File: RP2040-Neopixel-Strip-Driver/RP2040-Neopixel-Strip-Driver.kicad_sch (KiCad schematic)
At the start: 2 parts, among them U101 NLSX4302EBMUTCG

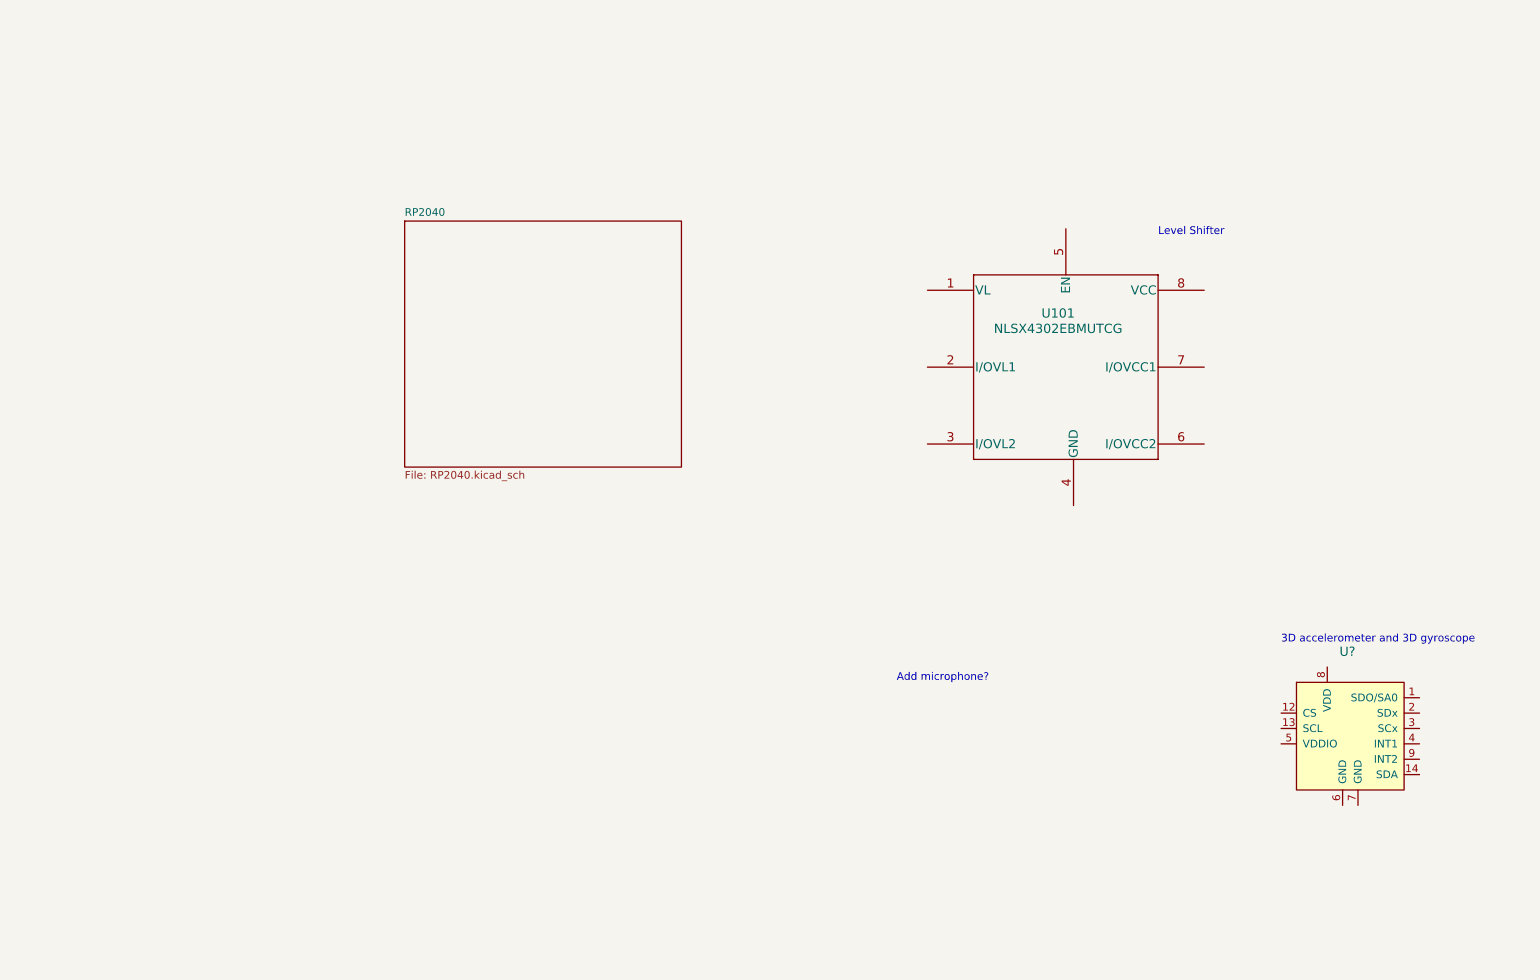
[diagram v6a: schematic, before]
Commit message: Project Expansion/Pivot - This is now a very involved cosplay prop tool.
Looking to incorporate a lot:
3D Gyro + 3D Accelerometer
Neopixel Driver
Speaker Driver
Microphone
SD Card Connector
Battery
Etc.
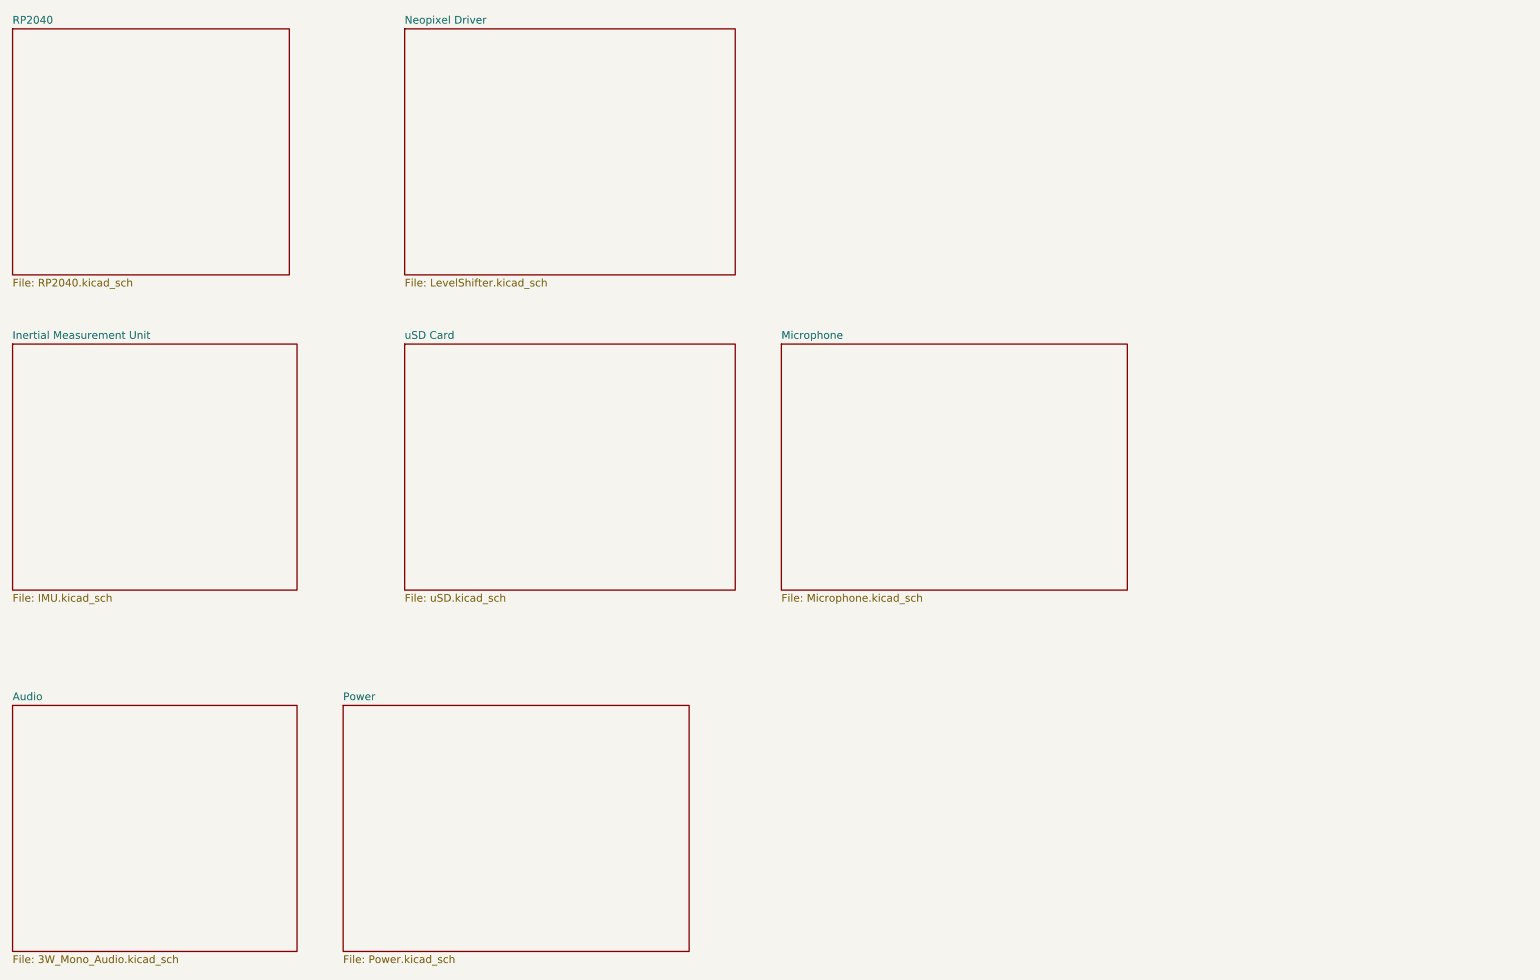
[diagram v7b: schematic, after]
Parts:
- removed U101: NLSX4302EBMUTCG, NLSX4302EBMUTCG:NLSX4302EBMUTCG, symbol NLSX4302EBMUTCG:NLSX4302EBMUTCG
- removed U?: (no value), symbol dk_Motion-Sensors-IMUs-Inertial-Measurement-Units:LSM6DS3TR
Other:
- added sheet Audio (3W_Mono_Audio.kicad_sch)
- added sheet Inertial Measurement Unit (IMU.kicad_sch)
- added sheet Microphone (Microphone.kicad_sch)
- added sheet Neopixel Driver (LevelShifter.kicad_sch)
- added sheet Power (Power.kicad_sch)
- added sheet uSD Card (uSD.kicad_sch)
- note removed: "3D accelerometer and 3D gyroscope"
- note removed: "Add microphone?"
- note removed: "Level Shifter"
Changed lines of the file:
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@@
     (comment 4 "https://github.com/mrangen/RP2040-Dev-Board")
   )
-  (text "Add microphone?" (at 163.83 127 0)
-    (effects (font (size 1.27 1.27)) (justify left bottom))
-  )
-  (text "Level Shifter\n" (at 207.01 53.34 0)
-    (effects (font (size 1.27 1.27)) (justify left bottom))
-  )
-  (text "3D accelerometer and 3D gyroscope" (at 227.33 120.65 0)
-    (effects (font (size 1.27 1.27)) (justify left bottom))
-  )
-  (symbol (lib_id "NLSX4302EBMUTCG:NLSX4302EBMUTCG") (at 168.91 67.31 0) (unit 1)
-    (in_bom yes) (on_board yes) (fields_autoplaced)
-    (property "Reference" "U101" (id 0) (at 190.5 66.04 0)
-      (effects (font (size 1.524 1.524)))
-    )
-    (property "Value" "NLSX4302EBMUTCG" (id 1) (at 190.5 68.58 0)
-      (effects (font (size 1.524 1.524)))
-    )
-    (property "Footprint" "NLSX4302EBMUTCG:NLSX4302EBMUTCG" (id 2) (at 191.77 58.674 0)
-      (effects (font (size 1.524 1.524)) hide)
-    )
-    (property "Datasheet" "" (id 3) (at 168.91 67.31 0)
-      (effects (font (size 1.524 1.524)))
-    )
-    (property "JLCPCB P/N" "C893527" (id 4) (at 168.91 67.31 0)
-      (effects (font (size 1.27 1.27)) hide)
-    )
-    (pin "1")
-    (pin "2")
-    (pin "3")
-    (pin "4")
-    (pin "5")
-    (pin "6")
-    (pin "7")
-    (pin "8")
-  )
-  (symbol (lib_id "dk_Motion-Sensors-IMUs-Inertial-Measurement-Units:LSM6DS3TR") (at 237.49 137.16 0) (unit 1)
-    (in_bom yes) (on_board yes) (fields_autoplaced)
-    (property "Reference" "U?" (id 0) (at 236.9694 121.92 0)
-      (effects (font (size 1.524 1.524)) (justify left))
-    )
-    (property "Value" "" (id 1) (at 236.9694 125.73 0)
-      (effects (font (size 1.524 1.524)) (justify left))
-    )
-    (property "Footprint" "" (id 2) (at 242.57 132.08 0)
-      (effects (font (size 1.524 1.524)) (justify left) hide)
-    )
-    (property "Datasheet" "http://www.st.com/content/ccc/resource/technical/document/datasheet/a3/f5/4f/ae/8e/44/41/d7/DM00133076.pdf/files/DM00133076.pdf/jcr:content/translations/en.DM00133076.pdf" (id 3) (at 242.57 129.54 0)
-      (effects (font (size 1.524 1.524)) (justify left) hide)
-    )
-    (property "Digi-Key_PN" "497-15383-1-ND" (id 4) (at 242.57 127 0)
-      (effects (font (size 1.524 1.524)) (justify left) hide)
-    )
-    (property "MPN" "LSM6DS3TR" (id 5) (at 242.57 124.46 0)
-      (effects (font (size 1.524 1.524)) (justify left) hide)
-    )
-    (property "Category" "Sensors, Transducers" (id 6) (at 242.57 121.92 0)
-      (effects (font (size 1.524 1.524)) (justify left) hide)
-    )
-    (property "Family" "Motion Sensors - IMUs (Inertial Measurement Units)" (id 7) (at 242.57 119.38 0)
-      (effects (font (size 1.524 1.524)) (justify left) hide)
-    )
-    (property "DK_Datasheet_Link" "http://www.st.com/content/ccc/resource/technical/document/datasheet/a3/f5/4f/ae/8e/44/41/d7/DM00133076.pdf/files/DM00133076.pdf/jcr:content/translations/en.DM00133076.pdf" (id 8) (at 242.57 116.84 0)
-      (effects (font (size 1.524 1.524)) (justify left) hide)
-    )
-    (property "DK_Detail_Page" "/product-detail/en/stmicroelectronics/LSM6DS3TR/497-15383-1-ND/5180534" (id 9) (at 242.57 114.3 0)
-      (effects (font (size 1.524 1.524)) (justify left) hide)
-    )
-    (property "Description" "IMU ACCEL/GYRO I2C/SPI 14VFLGA" (id 10) (at 242.57 111.76 0)
-      (effects (font (size 1.524 1.524)) (justify left) hide)
-    )
-    (property "Manufacturer" "STMicroelectronics" (id 11) (at 242.57 109.22 0)
-      (effects (font (size 1.524 1.524)) (justify left) hide)
-    )
-    (property "Status" "Active" (id 12) (at 242.57 106.68 0)
-      (effects (font (size 1.524 1.524)) (justify left) hide)
-    )
-    (property "JLCPCB P/N" "C967633" (id 13) (at 237.49 137.16 0)
-      (effects (font (size 1.27 1.27)) hide)
-    )
-    (pin "1")
-    (pin "10")
-    (pin "11")
-    (pin "12")
-    (pin "13")
-    (pin "14")
-    (pin "2")
-    (pin "3")
-    (pin "4")
-    (pin "5")
-    (pin "6")
-    (pin "7")
-    (pin "8")
-    (pin "9")
-  )
-  (sheet (at 82.55 50.8) (size 45.72 40.64) (fields_autoplaced)
-    (stroke (width 0.1524) (type solid) (color 0 0 0 0))
-    (fill (color 0 0 0 0.0000))
-    (property "Sheet name" "RP2040" (id 0) (at 82.55 50.0884 0)
-      (effects (font (size 1.27 1.27)) (justify left bottom))
-    )
-    (property "Sheet file" "RP2040.kicad_sch" (id 1) (at 82.55 92.0246 0)
+  (sheet (at 17.78 130.81) (size 46.99 40.64) (fields_autoplaced)
+    (stroke (width 0.1524) (type solid) (color 0 0 0 0))
+    (fill (color 0 0 0 0.0000))
+    (property "Sheet name" "Audio" (id 0) (at 17.78 130.0984 0)
+      (effects (font (size 1.27 1.27)) (justify left bottom))
+    )
+    (property "Sheet file" "3W_Mono_Audio.kicad_sch" (id 1) (at 17.78 172.0346 0)
+      (effects (font (size 1.27 1.27)) (justify left top))
+    )
+  )
+  (sheet (at 72.39 130.81) (size 57.15 40.64) (fields_autoplaced)
+    (stroke (width 0.1524) (type solid) (color 0 0 0 0))
+    (fill (color 0 0 0 0.0000))
+    (property "Sheet name" "Power" (id 0) (at 72.39 130.0984 0)
+      (effects (font (size 1.27 1.27)) (justify left bottom))
+    )
+    (property "Sheet file" "Power.kicad_sch" (id 1) (at 72.39 172.0346 0)
+      (effects (font (size 1.27 1.27)) (justify left top))
+    )
+  )
+  (sheet (at 17.78 19.05) (size 45.72 40.64) (fields_autoplaced)
+    (stroke (width 0.1524) (type solid) (color 0 0 0 0))
+    (fill (color 0 0 0 0.0000))
+    (property "Sheet name" "RP2040" (id 0) (at 17.78 18.3384 0)
+      (effects (font (size 1.27 1.27)) (justify left bottom))
+    )
+    (property "Sheet file" "RP2040.kicad_sch" (id 1) (at 17.78 60.2746 0)
+      (effects (font (size 1.27 1.27)) (justify left top))
+    )
+  )
+  (sheet (at 17.78 71.12) (size 46.99 40.64) (fields_autoplaced)
+    (stroke (width 0.1524) (type solid) (color 0 0 0 0))
+    (fill (color 0 0 0 0.0000))
+    (property "Sheet name" "Inertial Measurement Unit" (id 0) (at 17.78 70.4084 0)
+      (effects (font (size 1.27 1.27)) (justify left bottom))
+    )
+    (property "Sheet file" "IMU.kicad_sch" (id 1) (at 17.78 112.3446 0)
+      (effects (font (size 1.27 1.27)) (justify left top))
+    )
+  )
+  (sheet (at 82.55 19.05) (size 54.61 40.64) (fields_autoplaced)
+    (stroke (width 0.1524) (type solid) (color 0 0 0 0))
+    (fill (color 0 0 0 0.0000))
+    (property "Sheet name" "Neopixel Driver" (id 0) (at 82.55 18.3384 0)
+      (effects (font (size 1.27 1.27)) (justify left bottom))
+    )
+    (property "Sheet file" "LevelShifter.kicad_sch" (id 1) (at 82.55 60.2746 0)
+      (effects (font (size 1.27 1.27)) (justify left top))
+    )
+  )
+  (sheet (at 144.78 71.12) (size 57.15 40.64) (fields_autoplaced)
+    (stroke (width 0.1524) (type solid) (color 0 0 0 0))
+    (fill (color 0 0 0 0.0000))
+    (property "Sheet name" "Microphone" (id 0) (at 144.78 70.4084 0)
+      (effects (font (size 1.27 1.27)) (justify left bottom))
+    )
+    (property "Sheet file" "Microphone.kicad_sch" (id 1) (at 144.78 112.3446 0)
+      (effects (font (size 1.27 1.27)) (justify left top))
+    )
+  )
+  (sheet (at 82.55 71.12) (size 54.61 40.64) (fields_autoplaced)
+    (stroke (width 0.1524) (type solid) (color 0 0 0 0))
+    (fill (color 0 0 0 0.0000))
+    (property "Sheet name" "uSD Card" (id 0) (at 82.55 70.4084 0)
+      (effects (font (size 1.27 1.27)) (justify left bottom))
+    )
+    (property "Sheet file" "uSD.kicad_sch" (id 1) (at 82.55 112.3446 0)
       (effects (font (size 1.27 1.27)) (justify left top))
     )
@@
     (path "/" (page "1"))
     (path "/3e7bcc2a-10c2-45cd-9897-4c0007e1c7fc" (page "2"))
+    (path "/70fbb85f-3163-4abc-9c0a-a891d94f22b1" (page "3"))
+    (path "/0a22e777-1680-4ad6-bc95-a4eb9dcd85fc" (page "4"))
+    (path "/0df4e21b-e0d5-4c43-99fc-07b3ff9e029e" (page "5"))
+    (path "/f6d3734f-f3ae-47ca-9988-e728219f2f3d" (page "6"))
+    (path "/7d3ce60b-0fbc-4d1c-8ad6-57910cd4368e" (page "7"))
+    (path "/84db7bec-6432-452c-8477-921546ad9ffb" (page "8"))
   )
   (symbol_instances
@@
       (reference "J206") (unit 1) (value "GND") (footprint "Connector_PinSocket_2.54mm:PinSocket_1x01_P2.54mm_Vertical")
     )
+    (path "/f6d3734f-f3ae-47ca-9988-e728219f2f3d/a52ed90b-9977-491a-b2c3-312cce74a18b"
+      (reference "MICRO_SD?") (unit 1) (value "TF-01A") (footprint "TF-01A")
+    )
     (path "/3e7bcc2a-10c2-45cd-9897-4c0007e1c7fc/97c99fad-afb5-471e-b90a-b7f0de492c8f"
       (reference "R201") (unit 1) (value "1k") (footprint "Breadstick Footprints:Perfect_0402_Resistor")
@@
       (reference "SW202") (unit 1) (value "~{USB_BOOT}") (footprint "Breadstick Footprints:GT-TC029B-H025-L1N")
     )
-    (path "/61abfe14-530f-45cb-bac5-bff48de16e05"
-      (reference "U101") (unit 1) (value "NLSX4302EBMUTCG") (footprint "NLSX4302EBMUTCG:NLSX4302EBMUTCG")
-    )
     (path "/3e7bcc2a-10c2-45cd-9897-4c0007e1c7fc/00c3344e-81e0-498f-aca3-32f690281efd"
       (reference "U201") (unit 1) (value "XC6206P332MR") (footprint "Package_TO_SOT_SMD:SOT-23")
@@
       (reference "U205") (unit 1) (value "W25Q128JVPIQ") (footprint "Package_SON:WSON-8-1EP_6x5mm_P1.27mm_EP3.4x4.3mm")
     )
-    (path "/e57cd689-f3bf-4a84-b820-dd33af7d6263"
+    (path "/70fbb85f-3163-4abc-9c0a-a891d94f22b1/cdfffdd0-a453-4bd1-a6a1-94448da82674"
       (reference "U?") (unit 1) (value "LSM6DS3TR") (footprint "digikey-footprints:LGA-14L_2.5x3mm__LSM6DS3")
     )
+    (path "/7d3ce60b-0fbc-4d1c-8ad6-57910cd4368e/fde06394-20cf-471d-939a-9b94cd877da7"
+      (reference "U?") (unit 1) (value "NLSX4302EBMUTCG") (footprint "NLSX4302EBMUTCG:NLSX4302EBMUTCG")
+    )
     (path "/3e7bcc2a-10c2-45cd-9897-4c0007e1c7fc/2a22be26-a817-4ed8-b112-95aa7d11fc7c"
